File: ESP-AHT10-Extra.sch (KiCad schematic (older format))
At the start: 23 parts, among them J1 USB, SW1 RESET, SW2 PROG, U1 CH330N, U2 HT7233, U3 ESP-12, U4 AHT10, U5 USBLC6-2SC6

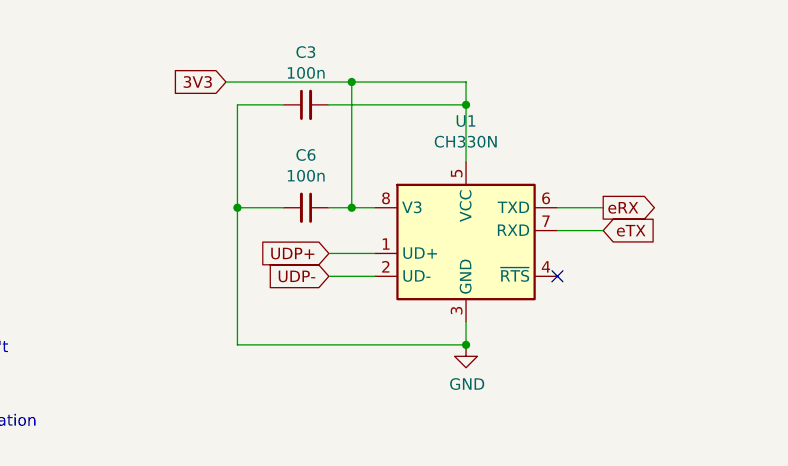
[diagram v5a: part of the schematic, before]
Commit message: switch CH300N to 5V, add 330R resistors to TX/RD, tweak GPIO0 connection, adjust ground connections
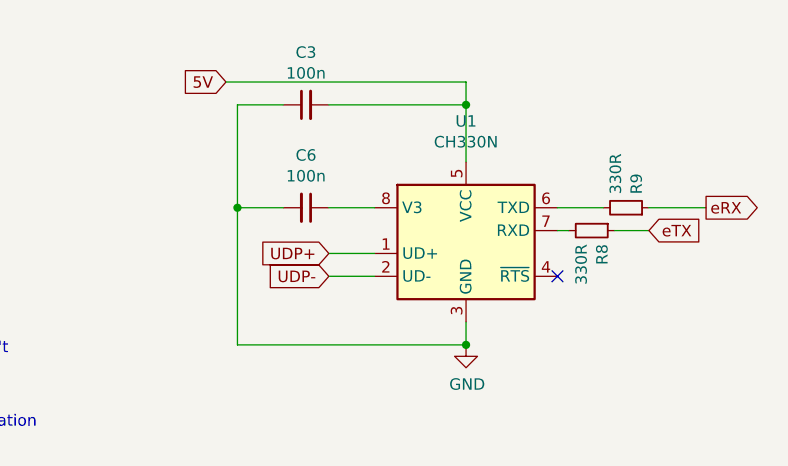
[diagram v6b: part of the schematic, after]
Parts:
- added R8, R9: 330R, Resistors_SMD:R_0805, symbol Device:R_Small
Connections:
- net 3V3: no longer C3.2, C6.1, U1.5 (VCC), U1.8 (V3)
- net 5V: now also C3.2, U1.5 (VCC)
- net eRX: now also R9.1; no longer U1.6 (TXD)
- net eTX: now also R8.1; no longer U1.7 (RXD)
- new net: R9.2, U1.6 (TXD)
- new net: R8.2, U1.7 (RXD)
- new net: C6.1, U1.8 (V3)
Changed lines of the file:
@@
 	1    0    0    -1
 $EndComp
-Text GLabel 7550 1100 0    50   Input ~ 0
-3V3
 Wire Wire Line
 	8600 1100 8600 1200
@@
 	8600 2150 8600 2250
 Connection ~ 8600 2250
-Text GLabel 9200 1750 2    50   Input ~ 0
+Text GLabel 9400 1750 2    50   Input ~ 0
 eTX
-Text GLabel 9200 1650 2    50   Output ~ 0
+Text GLabel 9650 1650 2    50   Output ~ 0
 eRX
-Wire Wire Line
-	9000 1650 9200 1650
-Wire Wire Line
-	9000 1750 9200 1750
 $Comp
 L Switch:SW_Push SW2
@@
 	0    1    1    0
 $EndComp
-Wire Wire Line
-	8000 1650 8100 1650
 $Comp
 L power:GND #PWR0101
@@
 NOTE: maybe overkill; I can't\nfind an example of a board\nwith WCH chips and ESD\nprotection. Apparently WCH\nchips have on-board termination\nresistors.
 Wire Wire Line
-	8100 1650 8100 1100
-Connection ~ 8100 1650
-Wire Wire Line
-	8100 1650 8200 1650
-Connection ~ 8100 1100
-Wire Wire Line
-	8100 1100 8600 1100
-Wire Wire Line
-	7550 1100 8100 1100
-Wire Wire Line
 	7600 1200 7800 1200
-Wire Wire Line
-	7600 1200 7600 1650
 Wire Wire Line
 	8000 1200 8600 1200
@@
 Wire Wire Line
 	7800 1650 7600 1650
+Wire Wire Line
+	7600 1650 7600 2250
+$Comp
+L Device:R_Small R8
+U 1 1 5DC99AD6
+P 9150 1750
+F 0 "R8" H 9209 1796 50  0000 L CNN
+F 1 "330R" H 9209 1705 50  0000 L CNN
+F 2 "Resistors_SMD:R_0805" H 9150 1750 50  0001 C CNN
+F 3 "~" H 9150 1750 50  0001 C CNN
+	1    9150 1750
+	0    1    1    0
+$EndComp
+$Comp
+L Device:R_Small R9
+U 1 1 5DC99C49
+P 9300 1650
+F 0 "R9" H 9359 1696 50  0000 L CNN
+F 1 "330R" H 9359 1605 50  0000 L CNN
+F 2 "Resistors_SMD:R_0805" H 9300 1650 50  0001 C CNN
+F 3 "~" H 9300 1650 50  0001 C CNN
+	1    9300 1650
+	0    1    -1   0
+$EndComp
+Wire Wire Line
+	9400 1650 9650 1650
+Wire Wire Line
+	9250 1750 9400 1750
+Wire Wire Line
+	9000 1650 9200 1650
+Wire Wire Line
+	9000 1750 9050 1750
+Wire Wire Line
+	8000 1650 8200 1650
+Wire Wire Line
+	7550 1100 8600 1100
+Text GLabel 7550 1100 0    50   Input ~ 0
+5V
+Wire Wire Line
+	7600 1200 7600 1650
 Connection ~ 7600 1650
-Wire Wire Line
-	7600 1650 7600 2250
 $EndSCHEMATC

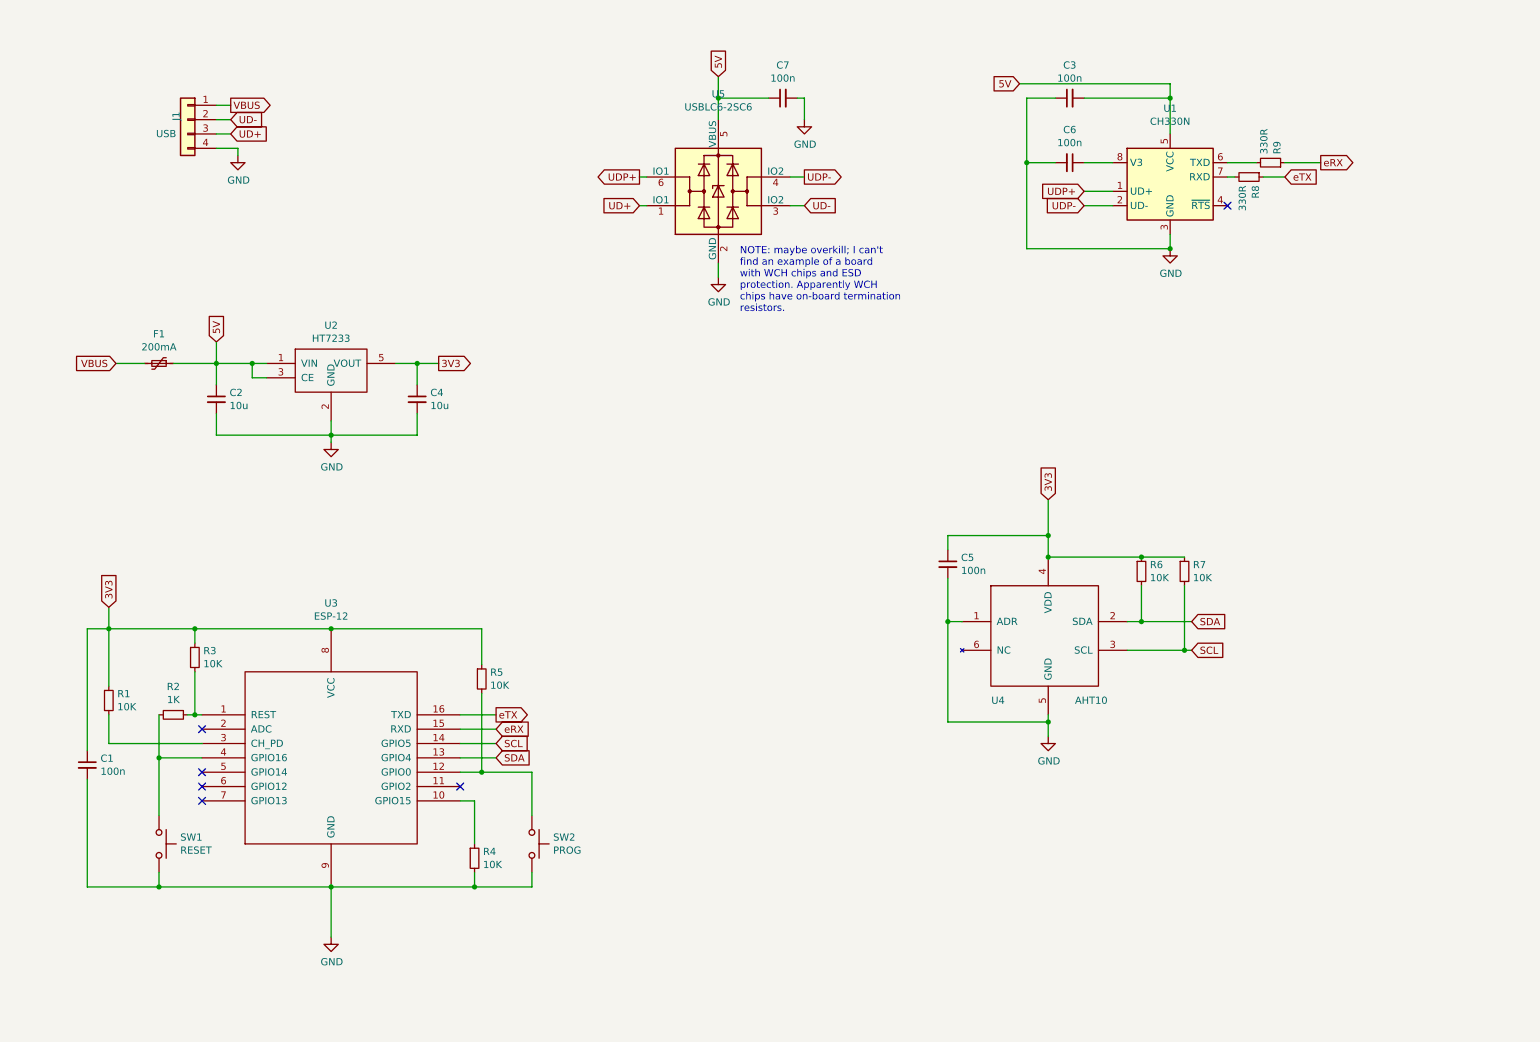
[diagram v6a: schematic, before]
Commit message: more fine tuning, layout cleanup, stability fixes
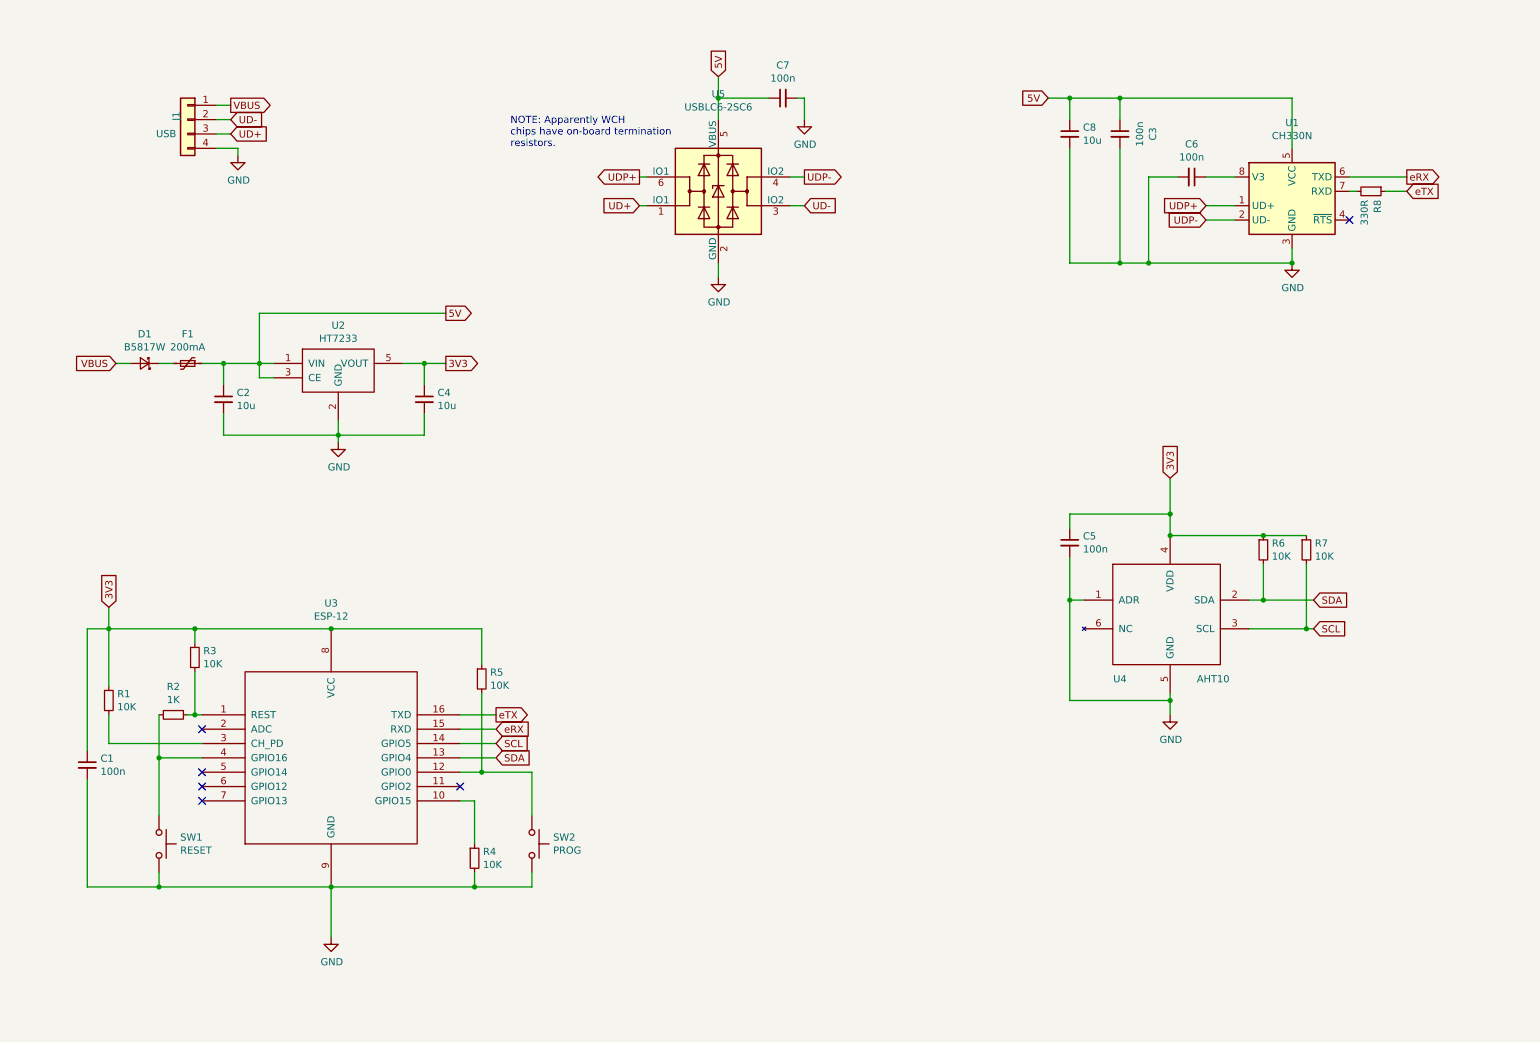
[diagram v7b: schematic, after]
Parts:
- removed R9: 330R, Resistors_SMD:R_0805, symbol Device:R_Small
- added C8: 10u, Capacitors_SMD:C_0805, symbol Device:C_Small
- added D1: B5817W, Diodes_SMD:D_SOD-123F, symbol Device:D_Schottky_Small
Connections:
- net 5V: now also C3.1, C8.1; no longer C3.2
- net GND: now also C3.2, C8.2; no longer C3.1
- net VBUS: now also D1.2 (A); no longer F1.2
- net eRX: now also U1.6 (TXD)
- new net: D1.1 (K), F1.2
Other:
- note added: "NOTE: Apparently WCH\nchips have on-board termination\nresistors."
- note removed: "NOTE: maybe overkill; I can't\nfind an example of a board\nwith WCH chips and ESD\nprotection. Apparently WCH\nchips have on-board termination\nresistors."
- moved on the sheet: C2, C3, C4, C5, C6, F1, R6, R7, R8, U1, U2, U4

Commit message: tidy up schematic, add some notes, etc.
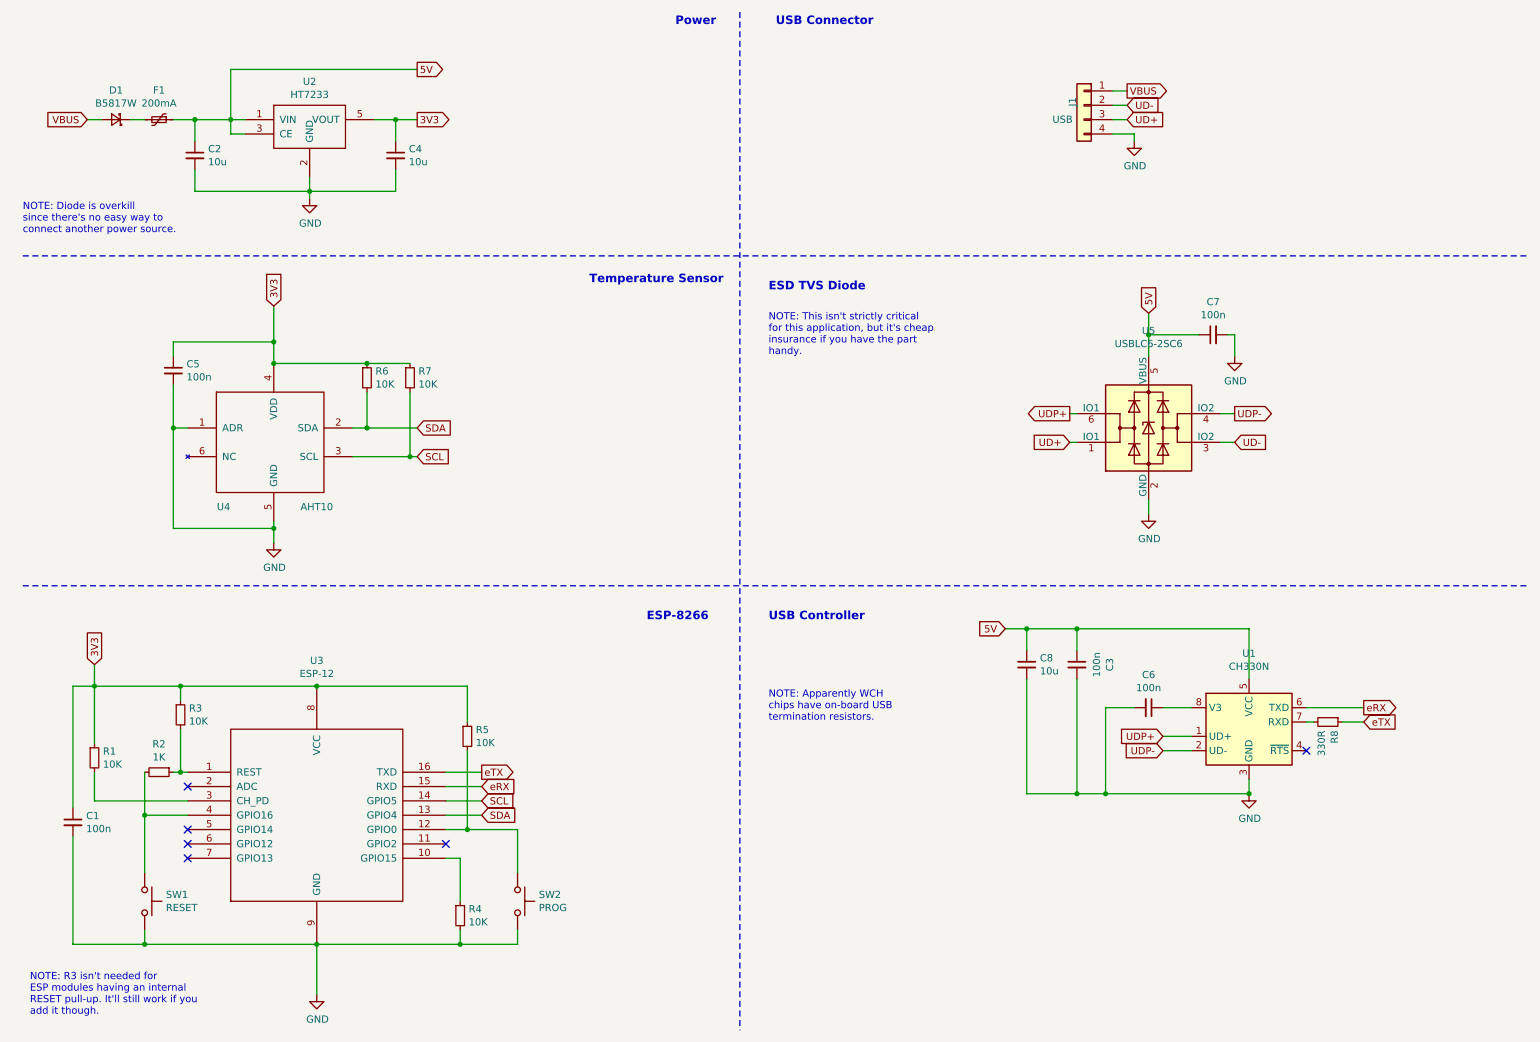
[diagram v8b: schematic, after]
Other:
- note added: "ESD TVS Diode"
- note added: "ESP-8266"
- note added: "NOTE: Apparently WCH\nchips have on-board USB\ntermination resistors."
- note added: "NOTE: Diode is overkill\nsince there's no easy way to\nconnect another power source."
- note added: "NOTE: R3 isn't needed for\nESP modules having an internal\nRESET pull-up. It'll still work if you\nadd it though."
- note added: "NOTE: This isn't strictly critical\nfor this application, but it's cheap\ninsurance if you have the part\nhandy."
- note added: "Power"
- note added: "Temperature Sensor"
- note added: "USB Connector"
- note added: "USB Controller"
- note removed: "NOTE: Apparently WCH\nchips have on-board termination\nresistors."
- moved on the sheet: C1, C2, C3, C4, C5, C6, C7, C8, D1, F1, J1, R1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
